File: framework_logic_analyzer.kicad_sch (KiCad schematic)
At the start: 63 parts, among them IC5 CYUSB3014-BZXC, J3 Conn_ARM_JTAG_SWD_10, Q1 MMBT3904, Q2 MMBT3904, Q3 MMBT3904, U5 M24M02-DR, Y1 19.200 MHz

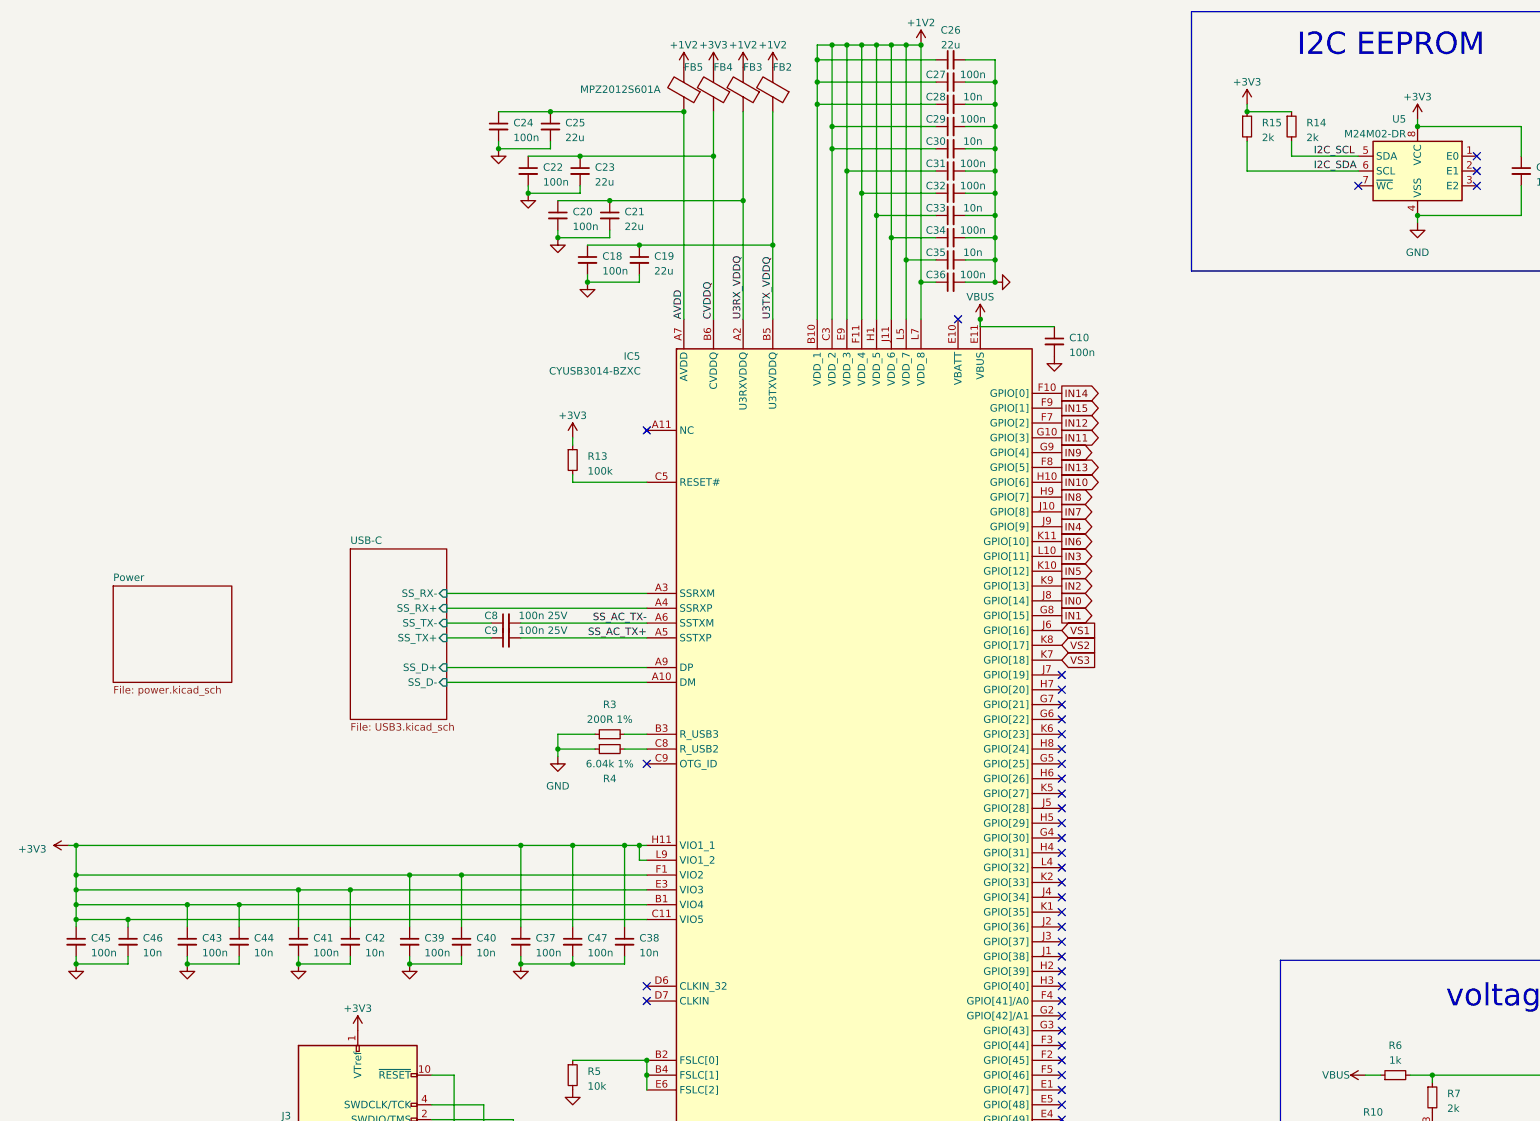
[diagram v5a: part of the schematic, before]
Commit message: implement USB3.0 active redriver and fix DRC errors
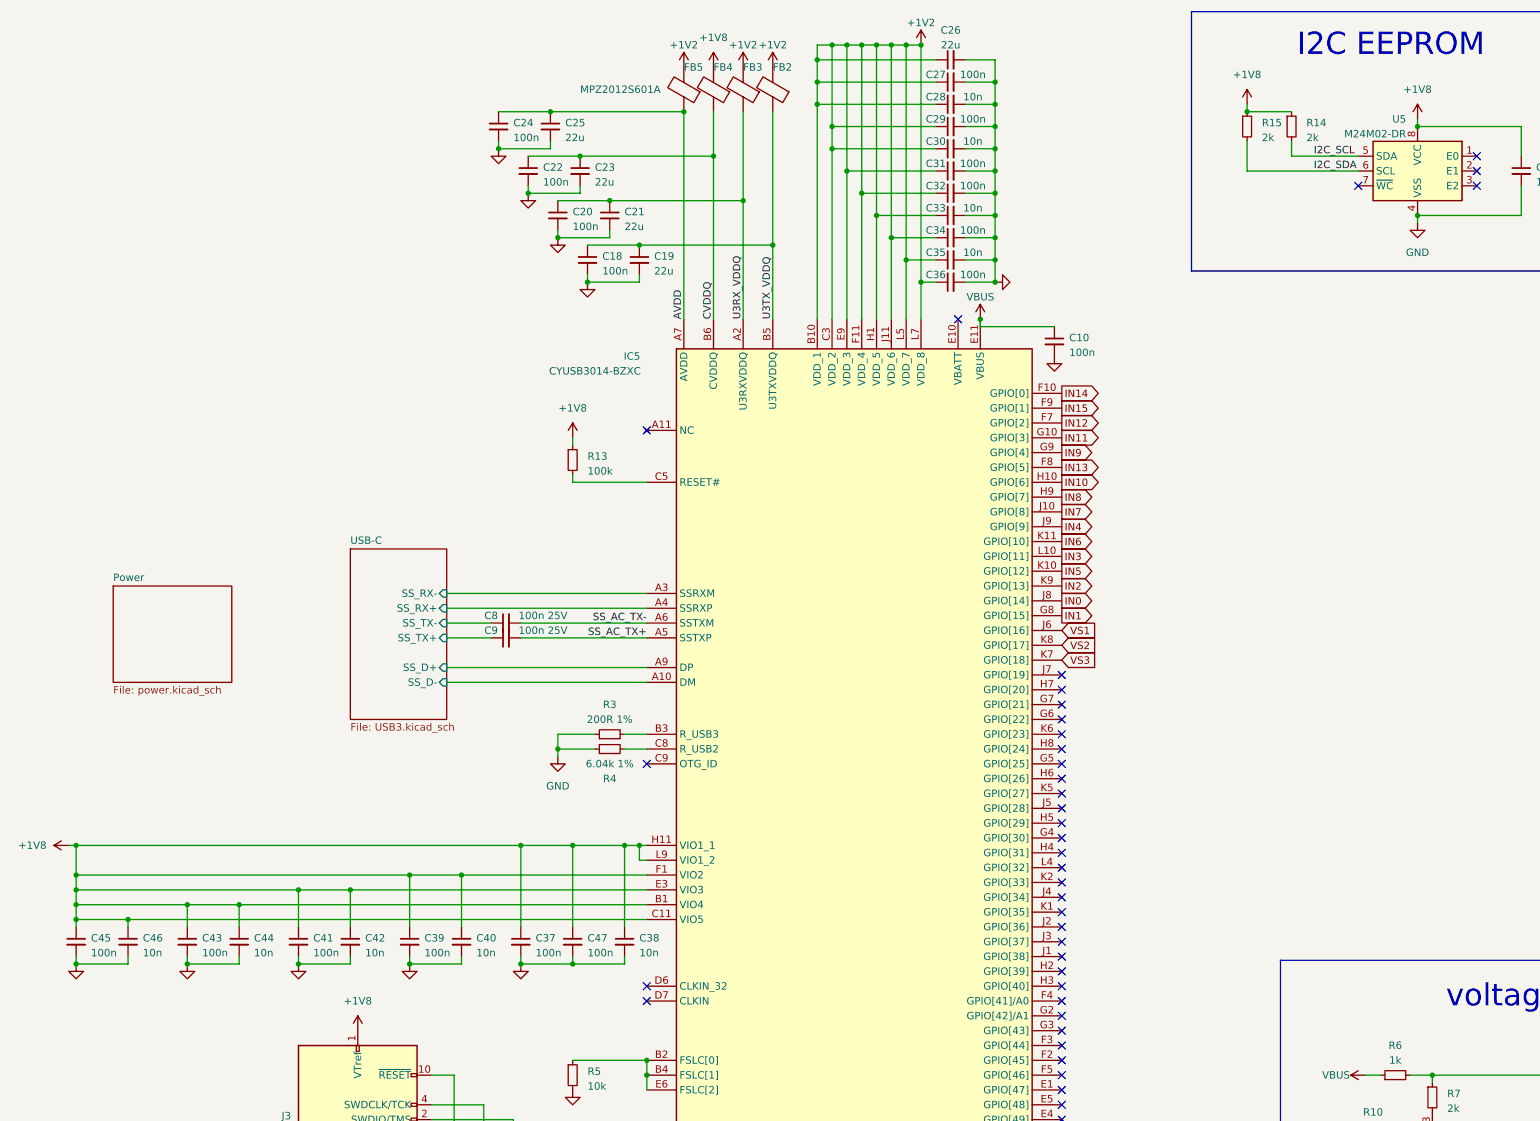
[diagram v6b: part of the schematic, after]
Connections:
- net +3V3 renamed +1V8

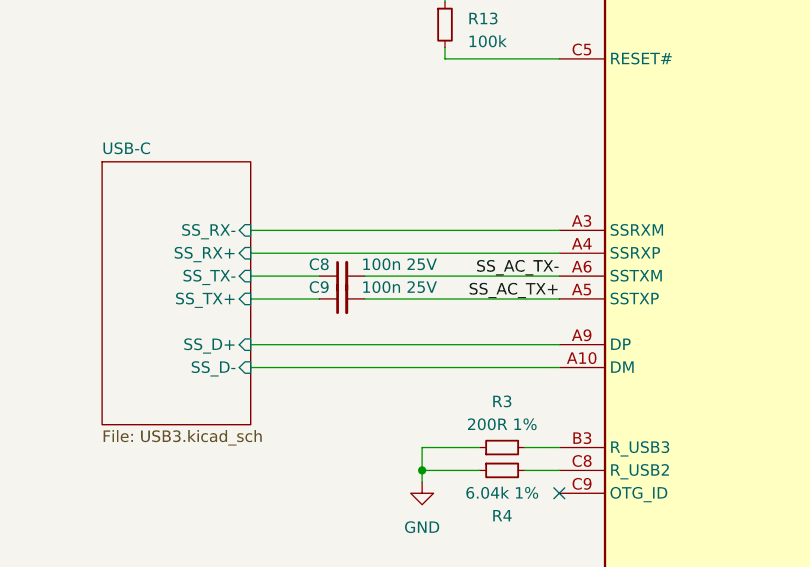
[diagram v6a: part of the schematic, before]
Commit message: add AC caps for redriver; fix ERC and DRC errors
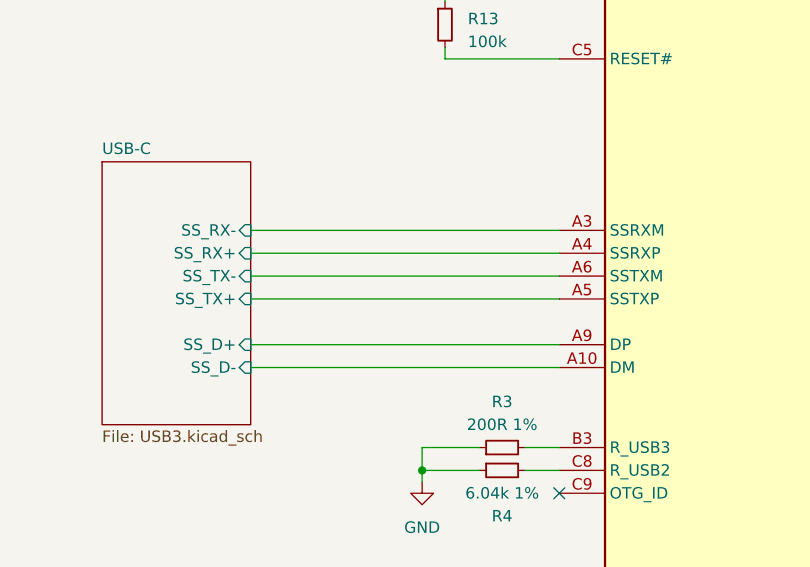
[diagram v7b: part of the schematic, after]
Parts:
- removed C8, C9: 100n 25V, Capacitor_SMD:C_0402_1005Metric, symbol Device:C_Small
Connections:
- net SS_AC_TX+ is gone; now on net USB-C/SS_TX+: IC5.A5 (SSTXP)
- net SS_AC_TX- is gone; now on net USB-C/SS_TX-: IC5.A6 (SSTXM)
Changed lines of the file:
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@@
 	(wire
 		(pts
-			(xy 86.36 118.11) (xy 93.98 118.11)
-		)
-		(stroke
-			(width 0)
-			(type default)
-		)
-	)
-	(wire
-		(pts
 			(xy 86.36 125.73) (xy 120.65 125.73)
 		)
@@
 	(wire
 		(pts
-			(xy 99.06 118.11) (xy 120.65 118.11)
-		)
-		(stroke
-			(width 0)
-			(type default)
-		)
-	)
-	(wire
-		(pts
 			(xy 171.45 243.84) (xy 173.99 243.84)
 		)
@@
 	(wire
 		(pts
+			(xy 86.36 120.65) (xy 120.65 120.65)
+		)
+		(stroke
+			(width 0)
+			(type default)
+		)
+	)
+	(wire
+		(pts
 			(xy 116.84 137.16) (xy 120.65 137.16)
 		)
@@
 	(wire
 		(pts
+			(xy 86.36 118.11) (xy 120.65 118.11)
+		)
+		(stroke
+			(width 0)
+			(type default)
+		)
+	)
+	(wire
+		(pts
 			(xy 105.41 137.16) (xy 105.41 139.7)
 		)
@@
 	(wire
 		(pts
-			(xy 120.65 120.65) (xy 99.06 120.65)
-		)
-		(stroke
-			(width 0)
-			(type default)
-		)
-	)
-	(wire
-		(pts
 			(xy 50.8 166.37) (xy 50.8 170.18)
 		)
@@
 	(wire
 		(pts
-			(xy 93.98 120.65) (xy 86.36 120.65)
-		)
-		(stroke
-			(width 0)
-			(type default)
-		)
-	)
-	(wire
-		(pts
 			(xy 31.75 176.53) (xy 22.86 176.53)
 		)
@@
 		)
 	)
-	(label "SS_AC_TX-"
-		(at 120.65 118.11 180)
-		(effects
-			(font
-				(size 1.27 1.27)
-			)
-			(justify right bottom)
-		)
-	)
 	(label "U3RX_VDDQ"
 		(at 137.16 66.04 90)
@@
 		)
 	)
-	(label "SS_AC_TX+"
-		(at 120.65 120.65 180)
-		(effects
-			(font
-				(size 1.27 1.27)
-			)
-			(justify right bottom)
-		)
-	)
 	(label "I2C_SDA"
 		(at 234.95 40.64 0)
@@
 					(unit 1)
 				)
-			)
-		)
-	)
-	(symbol
-		(lib_id "Device:C_Small")
-		(at 96.52 118.11 90)
-		(unit 1)
-		(exclude_from_sim no)
-		(in_bom yes)
-		(on_board yes)
-		(dnp no)
-		(property "Reference" "C8"
-			(at 93.98 116.84 90)
-			(effects
-				(font
-					(size 1.27 1.27)
-				)
-			)
-		)
-		(property "Value" "100n 25V"
-			(at 102.87 116.84 90)
-			(effects
-				(font
-					(size 1.27 1.27)
-				)
-			)
-		)
-		(property "Footprint" "Capacitor_SMD:C_0402_1005Metric"
-			(at 96.52 118.11 0)
-			(effects
-				(font
-					(size 1.27 1.27)
-				)
-				(hide yes)
-			)
-		)
-		(property "Datasheet" "~"
-			(at 96.52 118.11 0)
-			(effects
-				(font
-					(size 1.27 1.27)
-				)
-				(hide yes)
-			)
-		)
-		(property "Description" ""
-			(at 96.52 118.11 0)
-			(effects
-				(font
-					(size 1.27 1.27)
-				)
-			)
-		)
-		(pin "1"
-		)
-		(pin "2"
-		)
-		(instances
-			(project "framework_logic_analyzer"
-				(path "/cec59c69-8f0d-4d06-8fee-6cd1bb72d09c"
-					(reference "C8")
-					(unit 1)
-				)
-			)
-		)
-	)
-	(symbol
-		(lib_id "Device:C_Small")
-		(at 96.52 120.65 90)
-		(unit 1)
-		(exclude_from_sim no)
-		(in_bom yes)
-		(on_board yes)
-		(dnp no)
-		(property "Reference" "C9"
-			(at 93.98 119.38 90)
-			(effects
-				(font
-					(size 1.27 1.27)
-				)
-			)
-		)
-		(property "Value" "100n 25V"
-			(at 102.87 119.38 90)
-			(effects
-				(font
-					(size 1.27 1.27)
-				)
-			)
-		)
-		(property "Footprint" "Capacitor_SMD:C_0402_1005Metric"
-			(at 96.52 120.65 0)
-			(effects
-				(font
-					(size 1.27 1.27)
-				)
-				(hide yes)
-			)
-		)
-		(property "Datasheet" "~"
-			(at 96.52 120.65 0)
-			(effects
-				(font
-					(size 1.27 1.27)
-				)
-				(hide yes)
-			)
-		)
-		(property "Description" ""
-			(at 96.52 120.65 0)
-			(effects
-				(font
-					(size 1.27 1.27)
-				)
-			)
-		)
-		(pin "1"
-		)
-		(pin "2"
-		)
-		(instances
-			(project "framework_logic_analyzer"
-				(path "/cec59c69-8f0d-4d06-8fee-6cd1bb72d09c"
-					(reference "C9")
-					(unit 1)
-				)

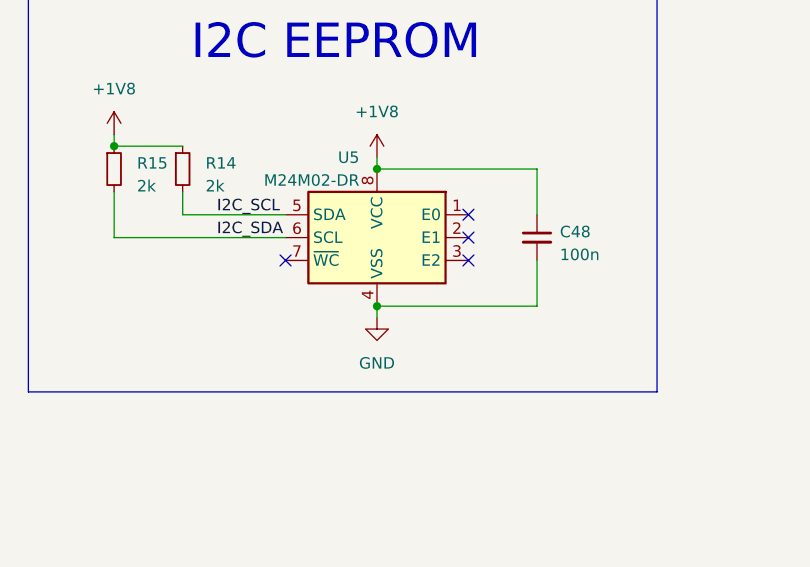
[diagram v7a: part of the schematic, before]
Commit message: start reworking the usb3c to add ESD and better impedance matching
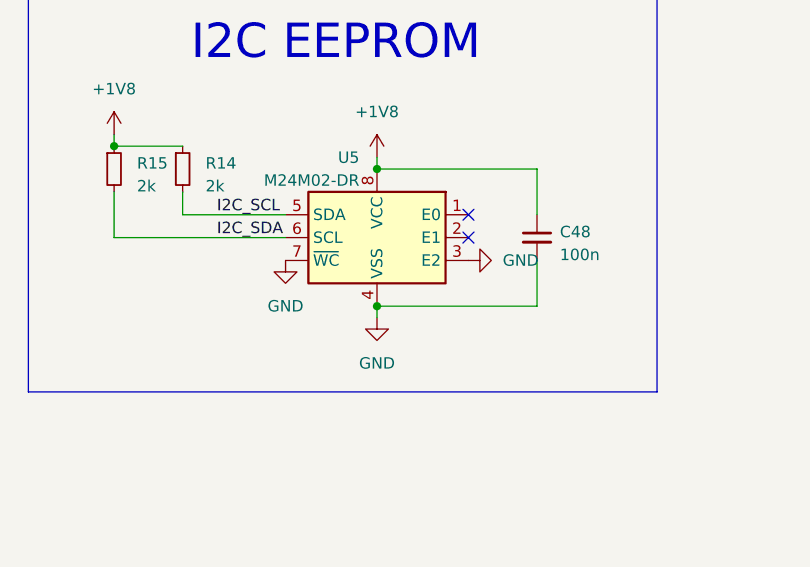
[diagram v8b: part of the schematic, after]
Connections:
- net GND: now also U5.3 (E2), U5.7 (~{WC})
- no-connect marks 50 -> 48
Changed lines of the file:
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@@
 	)
 	(no_connect
-		(at 262.89 38.1)
-	)
-	(no_connect
-		(at 262.89 43.18)
-	)
-	(no_connect
 		(at 191.77 162.56)
 	)
@@
 	)
 	(no_connect
-		(at 262.89 40.64)
-	)
-	(no_connect
 		(at 191.77 134.62)
 	)
@@
 	)
 	(no_connect
+		(at 262.89 38.1)
+	)
+	(no_connect
 		(at 191.77 193.04)
 	)
@@
 	)
 	(no_connect
-		(at 191.77 190.5)
+		(at 262.89 40.64)
 	)
 	(no_connect
-		(at 191.77 137.16)
+		(at 191.77 190.5)
 	)
 	(no_connect
-		(at 242.57 43.18)
+		(at 191.77 137.16)
 	)
 	(no_connect
@@
 	)
 	(symbol
+		(lib_id "power:GND")
+		(at 262.89 43.18 90)
+		(unit 1)
+		(exclude_from_sim no)
+		(in_bom yes)
+		(on_board yes)
+		(dnp no)
+		(fields_autoplaced yes)
+		(property "Reference" "#PWR010"
+			(at 269.24 43.18 0)
+			(effects
+				(font
+					(size 1.27 1.27)
+				)
+				(hide yes)
+			)
+		)
+		(property "Value" "GND"
+			(at 266.7 43.1799 90)
+			(effects
+				(font
+					(size 1.27 1.27)
+				)
+				(justify right)
+			)
+		)
+		(property "Footprint" ""
+			(at 262.89 43.18 0)
+			(effects
+				(font
+					(size 1.27 1.27)
+				)
+				(hide yes)
+			)
+		)
+		(property "Datasheet" ""
+			(at 262.89 43.18 0)
+			(effects
+				(font
+					(size 1.27 1.27)
+				)
+				(hide yes)
+			)
+		)
+		(property "Description" ""
+			(at 262.89 43.18 0)
+			(effects
+				(font
+					(size 1.27 1.27)
+				)
+			)
+		)
+		(pin "1"
+		)
+		(instances
+			(project "framework_logic_analyzer"
+				(path "/cec59c69-8f0d-4d06-8fee-6cd1bb72d09c"
+					(reference "#PWR010")
+					(unit 1)
+				)
+			)
+		)
+	)
+	(symbol
 		(lib_id "Device:C_Small")
 		(at 88.9 172.72 0)
@@
 					(unit 1)
 				)
+			)
+		)
+	)
+	(symbol
+		(lib_id "power:GND")
+		(at 242.57 43.18 0)
+		(unit 1)
+		(exclude_from_sim no)
+		(in_bom yes)
+		(on_board yes)
+		(dnp no)
+		(fields_autoplaced yes)
+		(property "Reference" "#PWR011"
+			(at 242.57 49.53 0)
+			(effects
+				(font
+					(size 1.27 1.27)
+				)
+				(hide yes)
+			)
+		)
+		(property "Value" "GND"
+			(at 242.57 48.26 0)
+			(effects
+				(font
+					(size 1.27 1.27)
+				)
+			)
+		)
+		(property "Footprint" ""
+			(at 242.57 43.18 0)
+			(effects
+				(font
+					(size 1.27 1.27)
+				)
+				(hide yes)
+			)
+		)
+		(property "Datasheet" ""
+			(at 242.57 43.18 0)
+			(effects
+				(font
+					(size 1.27 1.27)
+				)
+				(hide yes)
+			)
+		)
+		(property "Description" ""
+			(at 242.57 43.18 0)
+			(effects
+				(font
+					(size 1.27 1.27)
+				)
+			)
+		)
+		(pin "1"
+		)
+		(instances
+			(project "framework_logic_analyzer"
+				(path "/cec59c69-8f0d-4d06-8fee-6cd1bb72d09c"
+					(reference "#PWR011")
+					(unit 1)
+				)
